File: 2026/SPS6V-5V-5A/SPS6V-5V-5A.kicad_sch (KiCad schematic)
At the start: 17 parts, among them IC1 LMR51450, J1 VIN, J2 GND, J3 +5V, J4 GND

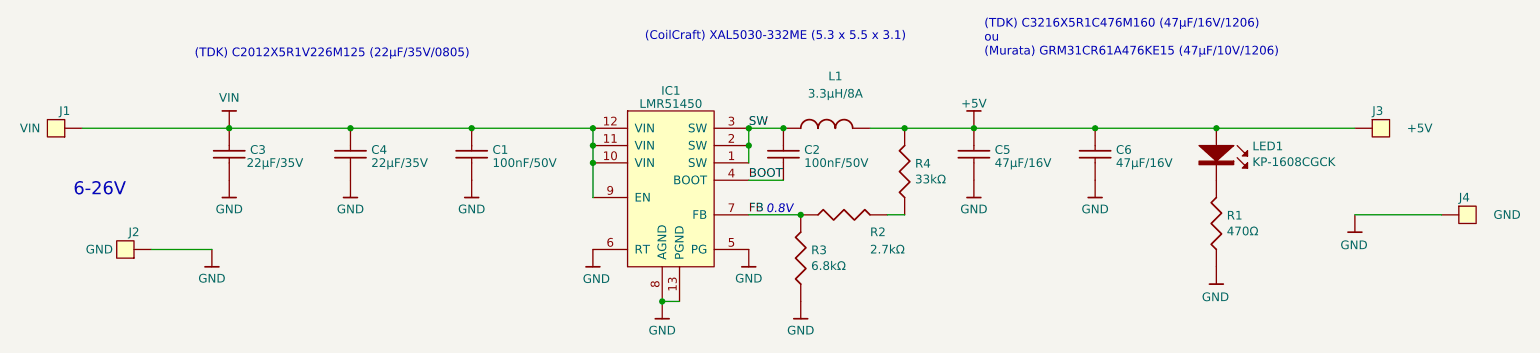
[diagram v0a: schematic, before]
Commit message: [alim 5V] remplace vias par footprint.
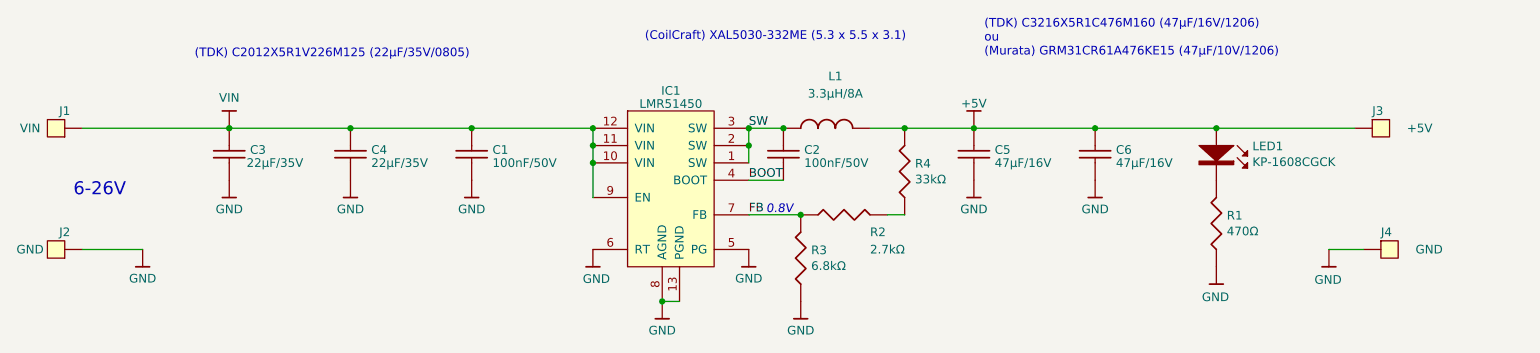
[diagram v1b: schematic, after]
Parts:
- J1, J2, J3, J4: footprint Library:PAD_5x5mm -> ENAC_robotique:power_PAD_THT
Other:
- moved on the sheet: J2, J4
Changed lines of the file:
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@@
 	(wire
 		(pts
-			(xy 236.22 83.82) (xy 248.92 83.82)
+			(xy 232.41 88.9) (xy 237.49 88.9)
 		)
 		(stroke
@@
 	(wire
 		(pts
-			(xy 59.69 88.9) (xy 68.58 88.9)
+			(xy 49.53 88.9) (xy 58.42 88.9)
 		)
 		(stroke
@@
 	(symbol
 		(lib_id "_GRZ_Power:GND")
-		(at 236.22 83.82 0)
+		(at 232.41 88.9 0)
 		(unit 1)
 		(exclude_from_sim no)
@@
 		(dnp no)
 		(property "Reference" "#PWR03"
-			(at 236.22 82.423 0)
+			(at 232.41 87.503 0)
 			(effects
 				(font
@@
 		)
 		(property "Value" "GND"
-			(at 236.093 88.265 0)
+			(at 232.283 93.345 0)
 			(effects
 				(font
@@
 		)
 		(property "Footprint" ""
-			(at 236.22 83.82 0)
-			(effects
-				(font
-					(size 1.27 1.27)
-				)
-				(hide yes)
-			)
-		)
-		(property "Datasheet" ""
-			(at 236.22 83.82 0)
-			(effects
-				(font
-					(size 1.27 1.27)
-				)
-				(hide yes)
-			)
-		)
-		(property "Description" ""
-			(at 236.22 83.82 0)
+			(at 232.41 88.9 0)
+			(effects
+				(font
+					(size 1.27 1.27)
+				)
+				(hide yes)
+			)
+		)
+		(property "Datasheet" ""
+			(at 232.41 88.9 0)
+			(effects
+				(font
+					(size 1.27 1.27)
+				)
+				(hide yes)
+			)
+		)
+		(property "Description" ""
+			(at 232.41 88.9 0)
 			(effects
 				(font
@@
 			)
 		)
-		(property "Footprint" "Library:PAD_5x5mm"
+		(property "Footprint" "ENAC_robotique:power_PAD_THT"
 			(at 240.03 72.39 0)
 			(effects
@@
 			)
 		)
-		(property "Footprint" "Library:PAD_5x5mm"
+		(property "Footprint" "ENAC_robotique:power_PAD_THT"
 			(at 45.72 69.85 0)
 			(effects
@@
 	(symbol
 		(lib_id "_GRZ_Connectors:CON01")
-		(at 59.69 88.9 180)
+		(at 49.53 88.9 180)
 		(unit 1)
 		(exclude_from_sim no)
@@
 		(dnp no)
 		(property "Reference" "J2"
-			(at 57.15 86.36 0)
+			(at 46.99 86.36 0)
 			(effects
 				(font
@@
 		)
 		(property "Value" "GND"
-			(at 52.07 88.9 0)
-			(effects
-				(font
-					(size 1.27 1.27)
-				)
-			)
-		)
-		(property "Footprint" "Library:PAD_5x5mm"
-			(at 55.88 87.63 0)
-			(effects
-				(font
-					(size 1.27 1.27)
-				)
-				(hide yes)
-			)
-		)
-		(property "Datasheet" ""
-			(at 55.88 87.63 0)
-			(effects
-				(font
-					(size 1.27 1.27)
-				)
-				(hide yes)
-			)
-		)
-		(property "Description" ""
-			(at 59.69 88.9 0)
+			(at 41.91 88.9 0)
+			(effects
+				(font
+					(size 1.27 1.27)
+				)
+			)
+		)
+		(property "Footprint" "ENAC_robotique:power_PAD_THT"
+			(at 45.72 87.63 0)
+			(effects
+				(font
+					(size 1.27 1.27)
+				)
+				(hide yes)
+			)
+		)
+		(property "Datasheet" ""
+			(at 45.72 87.63 0)
+			(effects
+				(font
+					(size 1.27 1.27)
+				)
+				(hide yes)
+			)
+		)
+		(property "Description" ""
+			(at 49.53 88.9 0)
 			(effects
 				(font
@@
 	(symbol
 		(lib_id "_GRZ_Connectors:CON01")
-		(at 248.92 83.82 0)
+		(at 237.49 88.9 0)
 		(unit 1)
 		(exclude_from_sim no)
@@
 		(dnp no)
 		(property "Reference" "J4"
-			(at 251.46 81.28 0)
+			(at 240.03 86.36 0)
 			(effects
 				(font
@@
 		)
 		(property "Value" "GND"
-			(at 256.54 83.82 0)
+			(at 245.11 88.9 0)
 			(effects
 				(font
@@
 			)
 		)
-		(property "Footprint" "Library:PAD_5x5mm"
-			(at 252.73 85.09 0)
-			(effects
-				(font
-					(size 1.27 1.27)
-				)
-				(hide yes)
-			)
-		)
-		(property "Datasheet" ""
-			(at 252.73 85.09 0)
-			(effects
-				(font
-					(size 1.27 1.27)
-				)
-				(hide yes)
-			)
-		)
-		(property "Description" ""
-			(at 248.92 83.82 0)
+		(property "Footprint" "ENAC_robotique:power_PAD_THT"
+			(at 241.3 90.17 0)
+			(effects
+				(font
+					(size 1.27 1.27)
+				)
+				(hide yes)
+			)
+		)
+		(property "Datasheet" ""
+			(at 241.3 90.17 0)
+			(effects
+				(font
+					(size 1.27 1.27)
+				)
+				(hide yes)
+			)
+		)
+		(property "Description" ""
+			(at 237.49 88.9 0)
 			(effects
 				(font
@@
 	(symbol
 		(lib_id "_GRZ_Power:GND")
-		(at 68.58 88.9 0)
+		(at 58.42 88.9 0)
 		(unit 1)
 		(exclude_from_sim no)
@@
 		(fields_autoplaced yes)
 		(property "Reference" "#PWR08"
-			(at 68.58 87.503 0)
+			(at 58.42 87.503 0)
 			(effects
 				(font
@@
 		)
 		(property "Value" "GND"
-			(at 68.58 93.1625 0)
+			(at 58.42 93.1625 0)
 			(effects
 				(font
@@
 		)
 		(property "Footprint" ""
-			(at 68.58 88.9 0)
-			(effects
-				(font
-					(size 1.27 1.27)
-				)
-				(hide yes)
-			)
-		)
-		(property "Datasheet" ""
-			(at 68.58 88.9 0)
-			(effects
-				(font
-					(size 1.27 1.27)
-				)
-				(hide yes)
-			)
-		)
-		(property "Description" ""
-			(at 68.58 88.9 0)
-			(effects
-				(font
+			(at 58.42 88.9 0)
+			(effects
+				(font
+					(size 1.27 1.27)
+				)
+				(hide yes)
+			)
+		)
+		(property "Datasheet" ""
+			(at 58.42 88.9 0)
+			(effects
+				(font
+					(size 1.27 1.27)
+				)
+				(hide yes)
+			)
+		)
+		(property "Description" ""
+			(at 58.42 88.9 0)
+			(effects
+				(font
